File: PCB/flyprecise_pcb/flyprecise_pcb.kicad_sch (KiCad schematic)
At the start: 4 parts, among them J1 Conn_01x08_Pin, J2 Conn_01x06_Pin, J3 Conn_01x10_Pin, J4 Conn_01x08_Pin

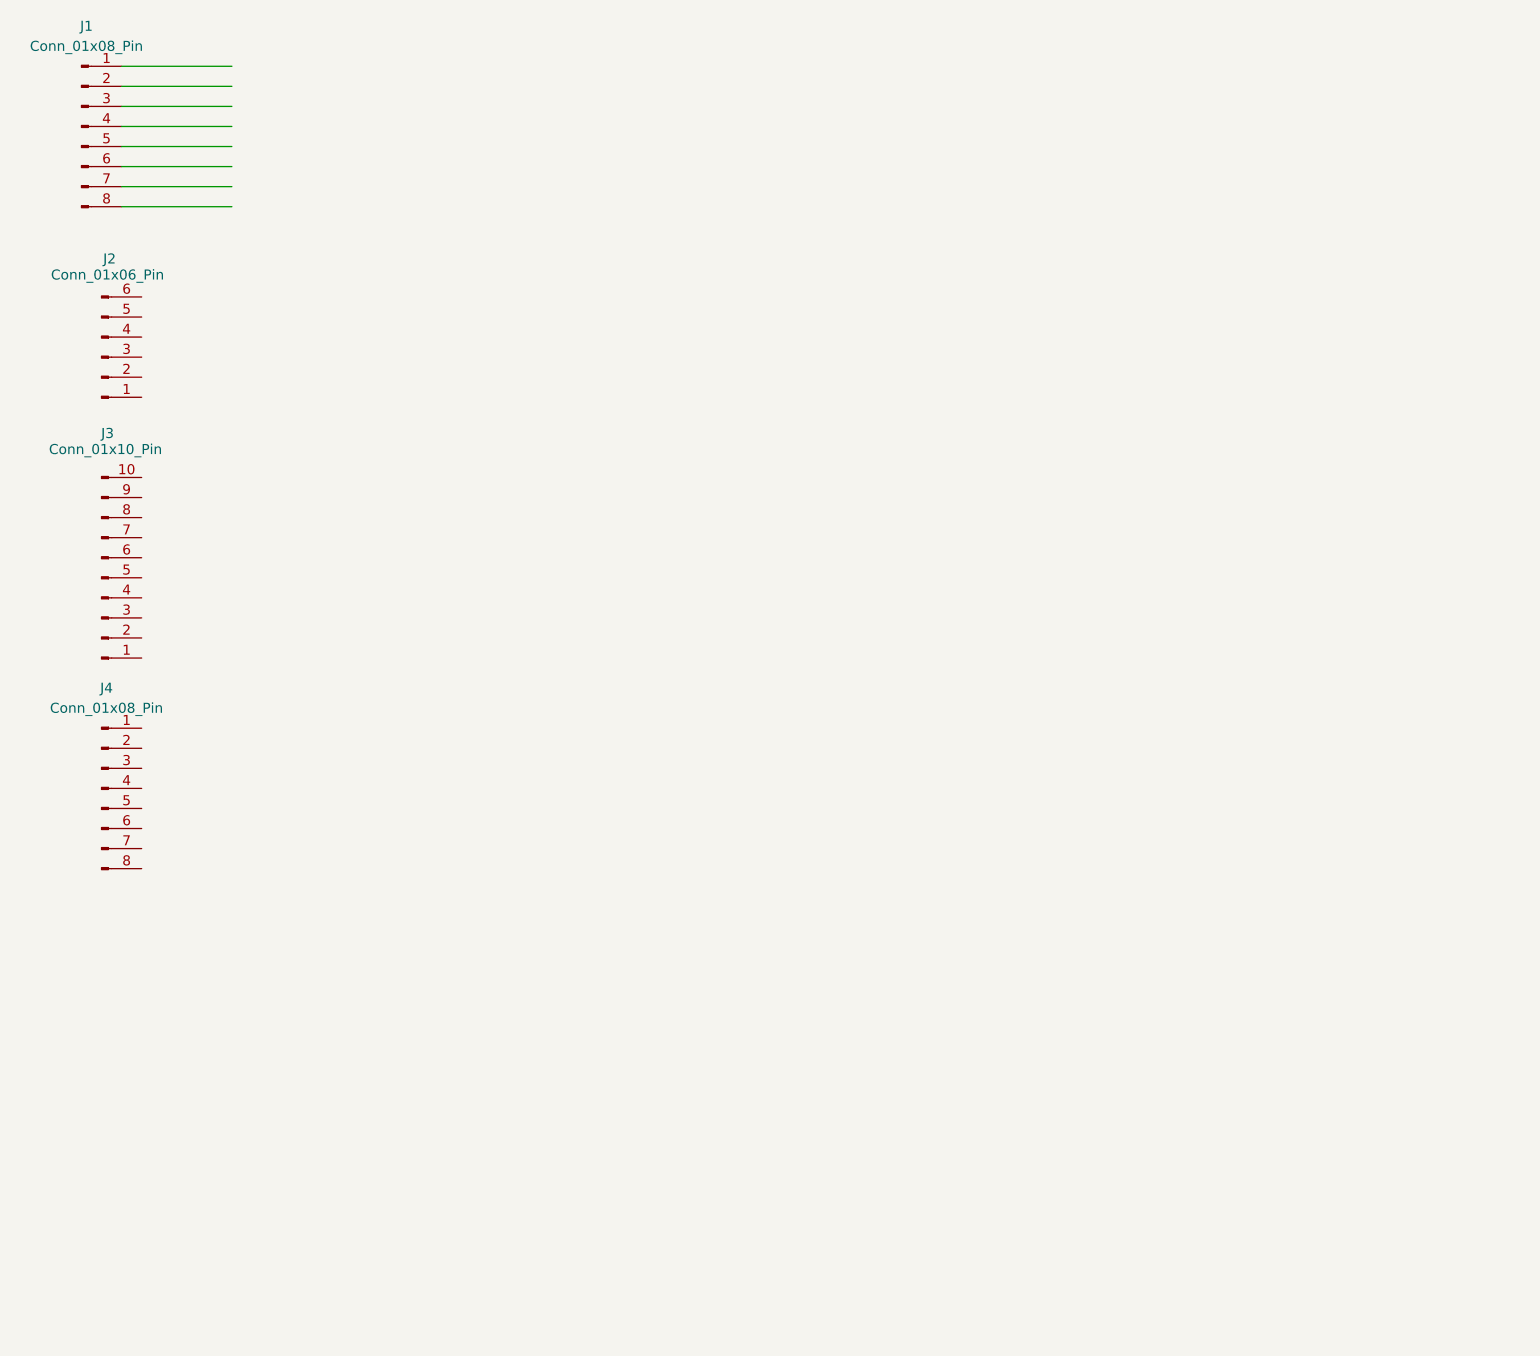
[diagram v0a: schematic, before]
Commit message: added to schematic
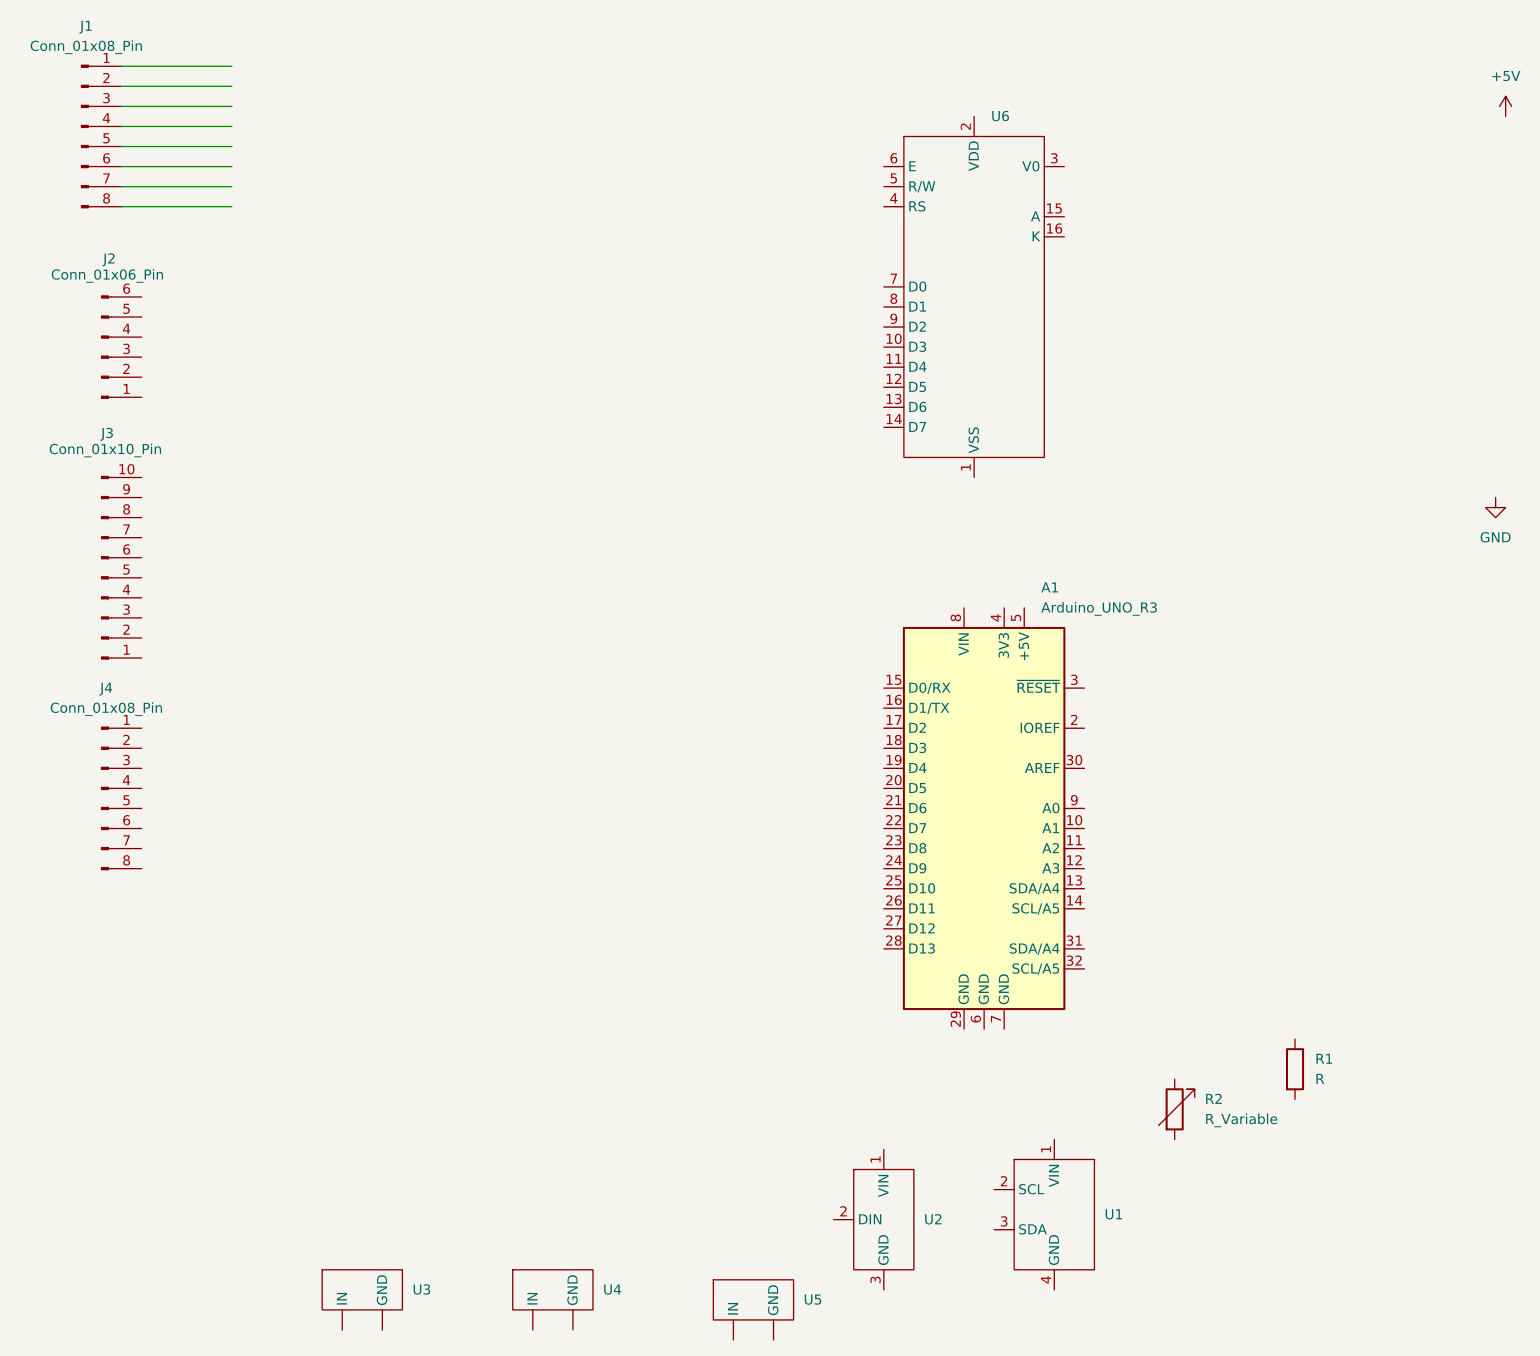
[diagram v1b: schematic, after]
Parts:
- added A1: Arduino_UNO_R3, Module:Arduino_UNO_R3, symbol MCU_Module:Arduino_UNO_R3
- added R1: R, Module:Arduino_UNO_R3, symbol Device:R
- added R2: R_Variable, symbol Device:R_Variable
- added U1: (no value), Sensor_Distance:ST_VL53L1x, symbol FP:VL53L0X_V2
- added U2: (no value), symbol FP:Flow_Meter
- added U3, U4, U5: (no value), symbol FP:MOSFET
- added U6: (no value), Display:LCD-016N002L, symbol FP:LCD1602_Module
